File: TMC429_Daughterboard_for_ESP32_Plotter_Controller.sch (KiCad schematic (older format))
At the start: 17 parts, among them J1 X Stepper A, J10 Y Limit, J11 X Limit, J2 X Stepper B, J3 X Stepper C, J4 Y Stepper A, J5 Y Stepper B, J6 Y Stepper C, J7 Z Motor, J8 Z_Limit, J9 Z Limit, U1 TMC2130, U2 TMC2130, U3 TMC429-BOB, U4 TMC2130

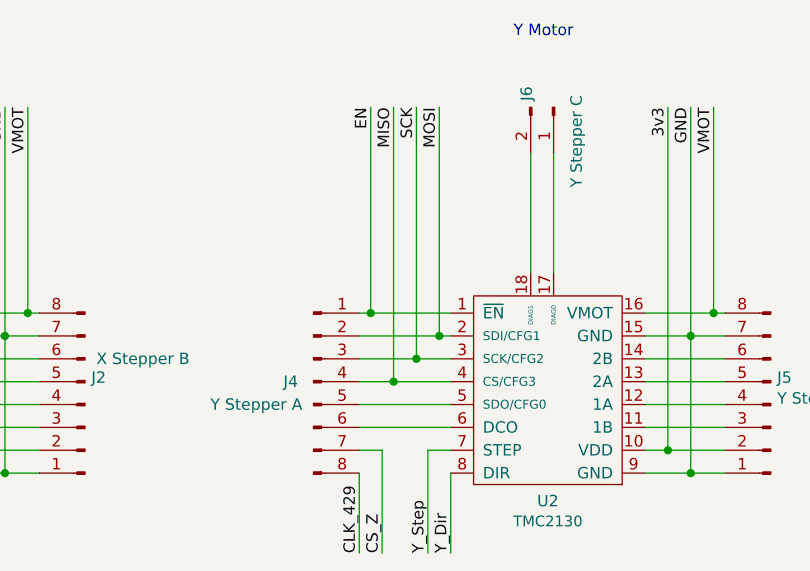
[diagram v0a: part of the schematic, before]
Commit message: Fix MISO/CS pins
Moved MISO to correct pin and updated Schematic and PCB.
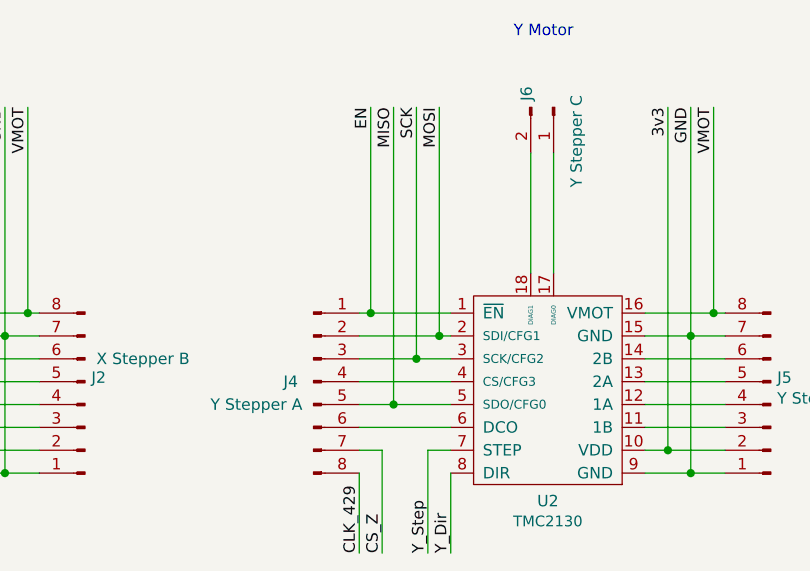
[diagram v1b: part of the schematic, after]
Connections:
- net MISO: now also J4.5 (Pin_5), U2.5 (SDO/CFG0); no longer J4.4 (Pin_4), U2.4 (CS/CFG3)
- new net: J4.4 (Pin_4), U2.4 (CS/CFG3)
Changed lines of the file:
@@
 	4950 2300 5200 2300
 Wire Wire Line
-	4950 2500 5350 2500
+	4950 2500 5100 2500
 Wire Wire Line
 	2200 2200 2200 1200
@@
 Wire Wire Line
 	1850 2400 2250 2400
-Wire Wire Line
-	4950 2400 5100 2400
 Text Notes 1750 3550 0    50   ~ 0
 TMC429 SPI Chip Select (was X_Dir)
@@
 Wire Wire Line
 	5200 2300 5350 2300
-Wire Wire Line
-	5100 2400 5100 1200
-Connection ~ 5100 2400
-Wire Wire Line
-	5100 2400 5350 2400
 Text Label 5100 1200 3    50   ~ 0
 MISO
@@
 Wire Wire Line
 	9350 2975 10550 2975
+Connection ~ 5100 2500
+Wire Wire Line
+	5100 2500 5350 2500
+Wire Wire Line
+	4950 2400 5350 2400
+Wire Wire Line
+	5100 1200 5100 2500
 $EndSCHEMATC
